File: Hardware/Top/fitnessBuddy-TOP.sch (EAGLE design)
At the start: 52 parts, among them SW3 SWITCH.MOM, SW4 SWITCH.MOM, U1 NRF52832_MODULE_MDBT42, U2 FT231XS

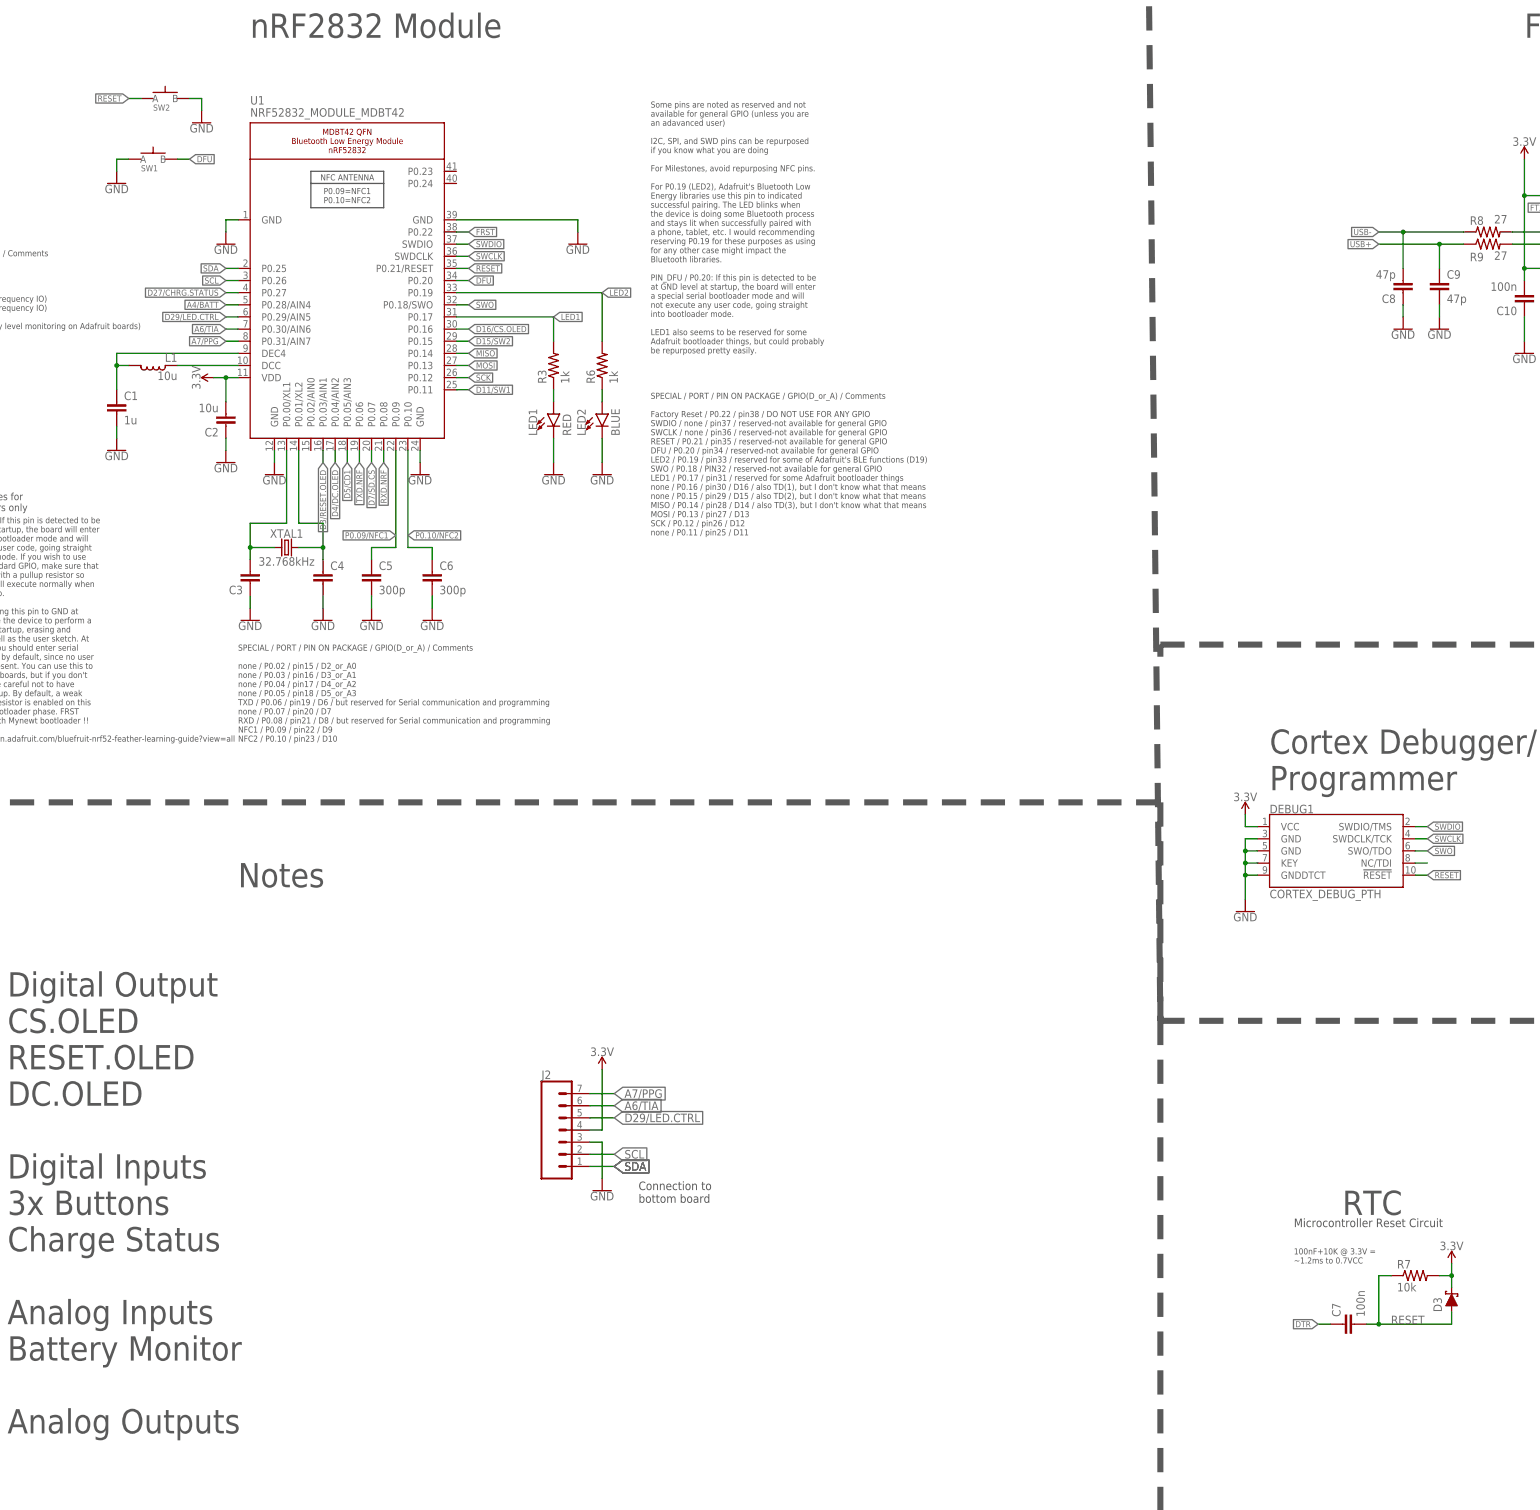
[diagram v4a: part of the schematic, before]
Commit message: routed top board
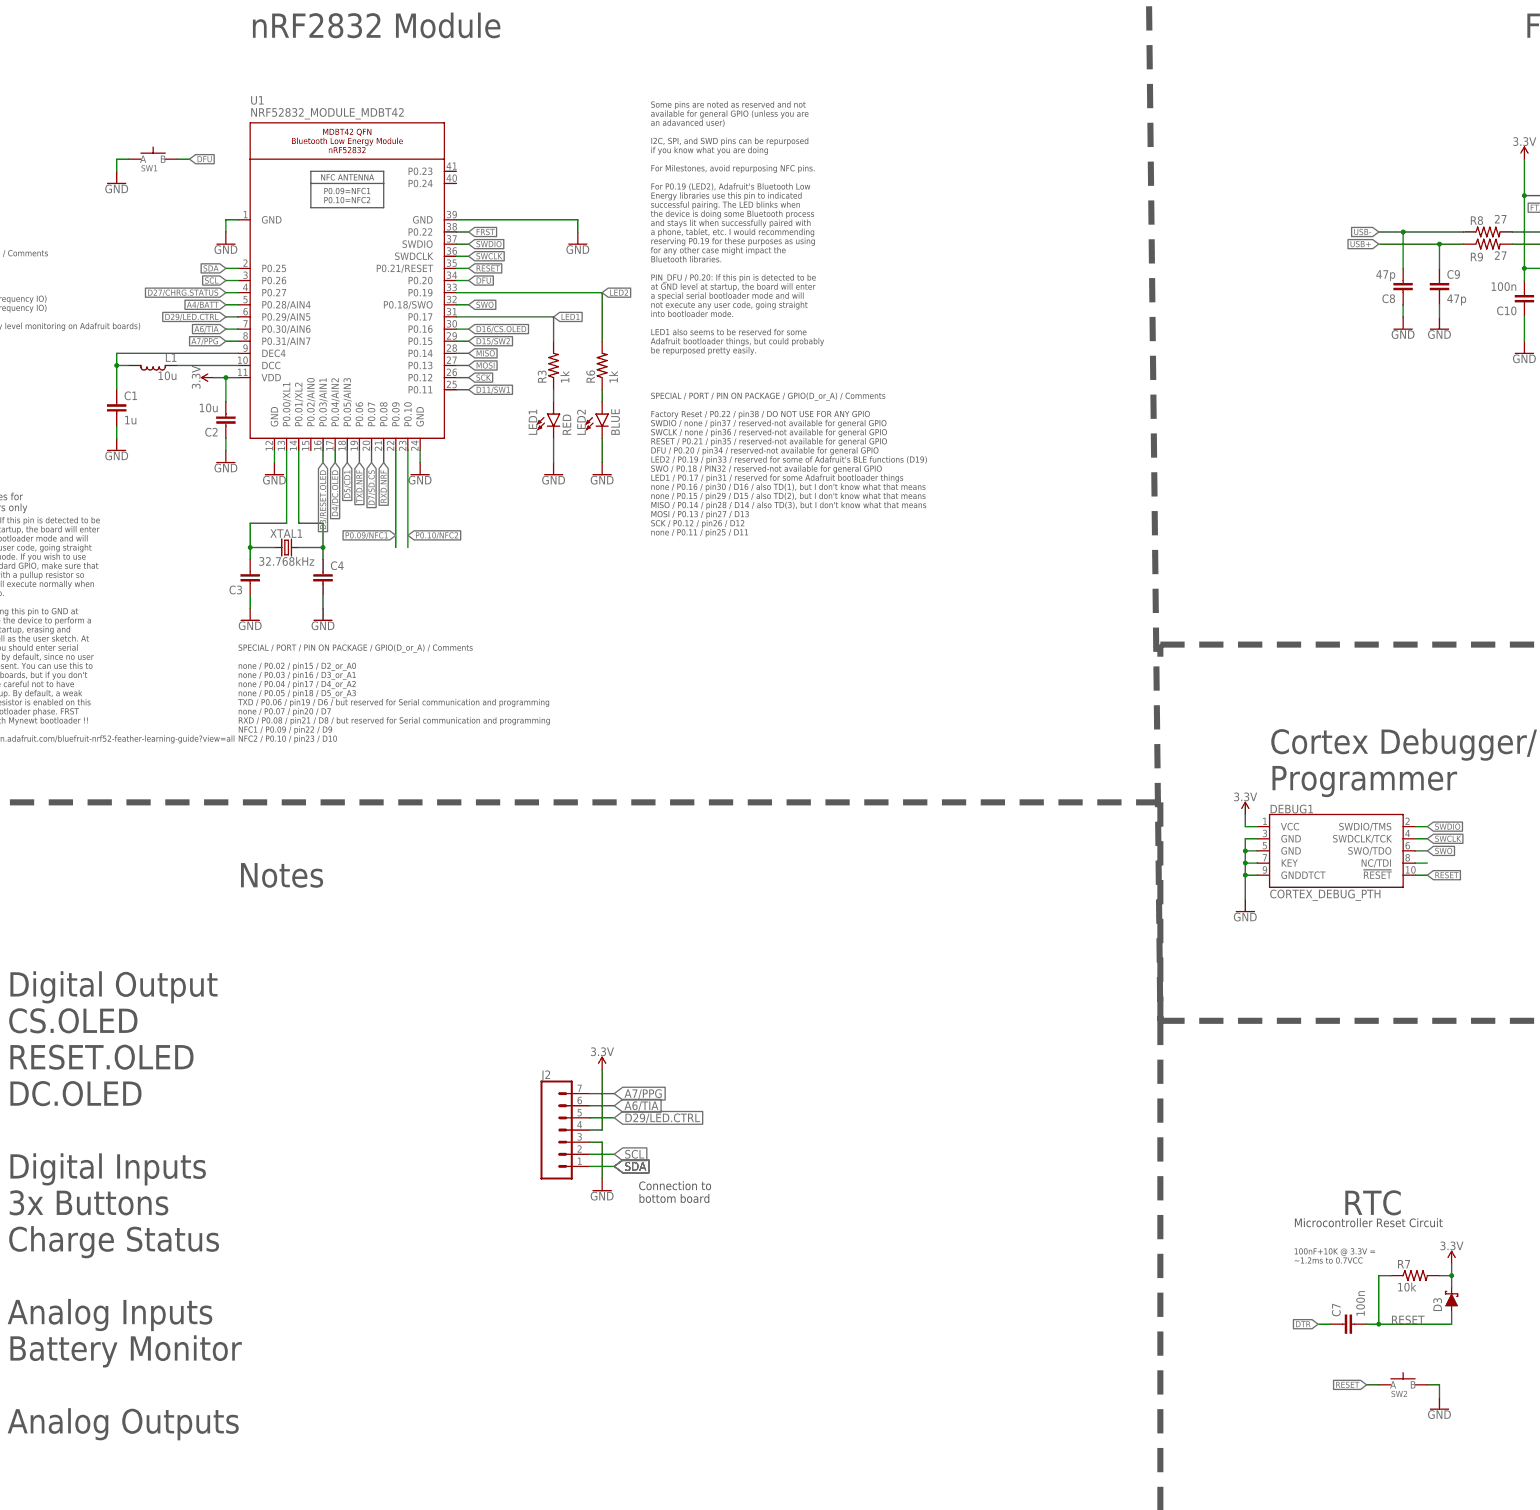
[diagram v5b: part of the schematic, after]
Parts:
- removed C5, C6: 300p, LinnesLab-Passives:CAPACITOR0603
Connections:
- net GND: no longer C5.2, C6.2
- net P0.09/NFC1: no longer C5.1
- net P0.10/NFC2: no longer C6.1
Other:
- moved on the sheet: SW2
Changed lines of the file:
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@@
 <part name="GND15" library="LinnesLab-Symbols" deviceset="GND" device=""/>
 <part name="GND16" library="LinnesLab-Symbols" deviceset="GND" device=""/>
-<part name="GND17" library="LinnesLab-Symbols" deviceset="GND" device=""/>
-<part name="GND18" library="LinnesLab-Symbols" deviceset="GND" device=""/>
 <part name="GND19" library="LinnesLab-Symbols" deviceset="GND" device=""/>
 <part name="GND20" library="LinnesLab-Symbols" deviceset="GND" device=""/>
@@
 <part name="C3" library="LinnesLab-Passives" deviceset="CAPACITOR" device="0603" package3d_urn="urn:adsk.eagle:package:15661989/2"/>
 <part name="C4" library="LinnesLab-Passives" deviceset="CAPACITOR" device="0603" package3d_urn="urn:adsk.eagle:package:15661989/2"/>
-<part name="C6" library="LinnesLab-Passives" deviceset="CAPACITOR" device="0603" package3d_urn="urn:adsk.eagle:package:15661989/2" value="300p"/>
-<part name="C5" library="LinnesLab-Passives" deviceset="CAPACITOR" device="0603" package3d_urn="urn:adsk.eagle:package:15661989/2" value="300p"/>
 <part name="C2" library="LinnesLab-Passives" deviceset="CAPACITOR" device="0805" package3d_urn="urn:adsk.eagle:package:15662010/2" value="10u"/>
 <part name="L1" library="LinnesLab-Passives" deviceset="INDUCTOR" device="0603" override_package3d_urn="urn:adsk.eagle:package:18592195/2" override_package_urn="urn:adsk.eagle:footprint:18592196/1" value="10u"/>
@@
 <attribute name="VALUE" x="53.34" y="335.026" size="1.778" layer="96" align="top-center"/>
 </instance>
-<instance part="GND17" gate="G$1" x="55.88" y="304.8" smashed="yes">
-<attribute name="VALUE" x="55.88" y="304.546" size="1.778" layer="96" align="top-center"/>
-</instance>
-<instance part="GND18" gate="G$1" x="43.18" y="304.8" smashed="yes">
-<attribute name="VALUE" x="43.18" y="304.546" size="1.778" layer="96" align="top-center"/>
-</instance>
 <instance part="GND19" gate="G$1" x="33.02" y="304.8" smashed="yes">
 <attribute name="VALUE" x="33.02" y="304.546" size="1.778" layer="96" align="top-center"/>
@@
 <attribute name="VALUE" x="34.544" y="310.261" size="1.778" layer="96"/>
 </instance>
-<instance part="C6" gate="G$1" x="55.88" y="312.42" smashed="yes">
-<attribute name="NAME" x="57.404" y="315.341" size="1.778" layer="95"/>
-<attribute name="VALUE" x="57.404" y="310.261" size="1.778" layer="96"/>
-</instance>
-<instance part="C5" gate="G$1" x="43.18" y="312.42" smashed="yes">
-<attribute name="NAME" x="44.704" y="315.341" size="1.778" layer="95"/>
-<attribute name="VALUE" x="44.704" y="310.261" size="1.778" layer="96"/>
-</instance>
 <instance part="C2" gate="G$1" x="12.7" y="347.98" smashed="yes" rot="R180">
 <attribute name="NAME" x="11.176" y="345.059" size="1.778" layer="95" rot="R180"/>
@@
 <attribute name="VALUE" x="269.24" y="172.974" size="1.778" layer="96" align="bottom-center"/>
 </instance>
-<instance part="GND28" gate="G$1" x="7.62" y="408.94" smashed="yes">
-<attribute name="VALUE" x="7.62" y="408.686" size="1.778" layer="96" align="top-center"/>
+<instance part="GND28" gate="G$1" x="266.7" y="139.7" smashed="yes">
+<attribute name="VALUE" x="266.7" y="139.446" size="1.778" layer="96" align="top-center"/>
 </instance>
 <instance part="SUPPLY5" gate="G$1" x="226.06" y="264.16" smashed="yes">
@@
 <attribute name="VALUE" x="22.86" y="335.026" size="1.778" layer="96" align="top-center"/>
 </instance>
-<instance part="SW2" gate="G$1" x="0" y="414.02" smashed="yes">
-<attribute name="NAME" x="-2.54" y="411.48" size="1.27" layer="95"/>
-<attribute name="VALUE" x="-2.54" y="408.94" size="1.27" layer="96"/>
+<instance part="SW2" gate="G$1" x="259.08" y="144.78" smashed="yes">
+<attribute name="NAME" x="256.54" y="142.24" size="1.27" layer="95"/>
+<attribute name="VALUE" x="256.54" y="139.7" size="1.27" layer="96"/>
 </instance>
 <instance part="U1" gate="G$1" x="38.1" y="375.92" smashed="yes">
@@
 </segment>
 <segment>
-<pinref part="C5" gate="G$1" pin="2"/>
-<pinref part="GND18" gate="G$1" pin="GND"/>
-<wire x1="43.18" y1="307.34" x2="43.18" y2="309.88" width="0.1524" layer="91"/>
-</segment>
-<segment>
-<pinref part="C6" gate="G$1" pin="2"/>
-<pinref part="GND17" gate="G$1" pin="GND"/>
-<wire x1="55.88" y1="307.34" x2="55.88" y2="309.88" width="0.1524" layer="91"/>
-</segment>
-<segment>
 <wire x1="15.24" y1="388.62" x2="12.7" y2="388.62" width="0.1524" layer="91"/>
 <wire x1="12.7" y1="388.62" x2="12.7" y2="386.08" width="0.1524" layer="91"/>
@@
 </segment>
 <segment>
-<wire x1="5.08" y1="414.02" x2="7.62" y2="414.02" width="0.1524" layer="91"/>
-<wire x1="7.62" y1="414.02" x2="7.62" y2="411.48" width="0.1524" layer="91"/>
+<wire x1="264.16" y1="144.78" x2="266.7" y2="144.78" width="0.1524" layer="91"/>
+<wire x1="266.7" y1="144.78" x2="266.7" y2="142.24" width="0.1524" layer="91"/>
 <pinref part="GND28" gate="G$1" pin="GND"/>
 <pinref part="SW2" gate="G$1" pin="B"/>
@@
 </segment>
 <segment>
-<wire x1="-7.62" y1="414.02" x2="-5.08" y2="414.02" width="0.1524" layer="91"/>
-<label x="-7.62" y="414.02" size="1.27" layer="95" rot="R180" xref="yes"/>
+<wire x1="251.46" y1="144.78" x2="254" y2="144.78" width="0.1524" layer="91"/>
+<label x="251.46" y="144.78" size="1.27" layer="95" rot="R180" xref="yes"/>
 <pinref part="SW2" gate="G$1" pin="A"/>
 </segment>
@@
 <segment>
 <wire x1="48.26" y1="340.36" x2="48.26" y2="320.04" width="0.1524" layer="91"/>
-<wire x1="43.18" y1="320.04" x2="48.26" y2="320.04" width="0.1524" layer="91"/>
-<wire x1="43.18" y1="320.04" x2="43.18" y2="317.5" width="0.1524" layer="91"/>
-<pinref part="C5" gate="G$1" pin="1"/>
 <pinref part="U1" gate="G$1" pin="P0.09"/>
 <label x="48.26" y="322.58" size="1.27" layer="95" rot="R180" xref="yes"/>
@@
 <segment>
 <wire x1="50.8" y1="340.36" x2="50.8" y2="320.04" width="0.1524" layer="91"/>
-<wire x1="50.8" y1="320.04" x2="55.88" y2="320.04" width="0.1524" layer="91"/>
-<wire x1="55.88" y1="320.04" x2="55.88" y2="317.5" width="0.1524" layer="91"/>
-<pinref part="C6" gate="G$1" pin="1"/>
 <pinref part="U1" gate="G$1" pin="P0.10"/>
 <label x="50.8" y="322.58" size="1.27" layer="95" xref="yes"/>

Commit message: finished halfway through take 007. organized board/ connected airwires
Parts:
- C13: device LinnesLab-Passives:CAPACITOR0402 -> LinnesLab-Passives:CAPACITOR0603
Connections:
- removed net !DTR: U2.!DTR
- removed net A4/BATT: R4.1, R5.2, U1.P0.28/AIN4
- removed net A6/TIA: J2.6, U1.P0.30/AIN6
- removed net A7/PPG: J2.7, U1.P0.31/AIN7
- removed net D29/LED.CTRL: J2.5, U1.P0.29/AIN5
- new net A4/PPG: J2.7, U1.P0.28/AIN4
- new net A5/TIA: J2.6, U1.P0.29/AIN5
- new net A7/BATT: R4.1, R5.2, U1.P0.31/AIN7
- new net D30/LED.CTRL: J2.5, U1.P0.30/AIN6
- net DTR: now also U2.!DTR
- net GND: no longer SW3.4, SW4.4

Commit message: organized top board
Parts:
- added C17, C18: 4.7u, LinnesLab-Passives:CAPACITOR0603
- added C5, C6: 1u, LinnesLab-Passives:CAPACITOR0603
- added CHRG2: MCP73831, LinnesLab-Power:MCP73831
- added LDO2: MIC5504, LinnesLab-Power:MIC5504
- added R16: (no value), LinnesLab-Passives:RESISTOR0603
- added R17: 100k, LinnesLab-Passives:RESISTOR0603
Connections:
- new net N$16: CHRG2.PROG, R16.2
- new net N$17: C18.2, CHRG2.VIN, R17.2
- net 3.3V: now also C6.1, LDO2.OUT
- net D27/CHRG.STATUS: now also CHRG2.STAT, R17.1
- net GND: now also C17.2, C18.1, C5.1, C6.2, CHRG2.VSS, LDO2.GND, R16.1
- net VIN: now also C5.2, LDO2.EN, LDO2.IN
- net VLIPO: now also C17.1, CHRG2.VBAT
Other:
- note added: "Digital Output"

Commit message: reorganized bottom boards, added RTC to bottom board, and added notes to top schematic
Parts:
- C10: value 100n -> 47p
- C11: value 10uF -> 47p
- C12: value 2.2uF -> 100n; device LinnesLab-Passives:CAPACITOR0402 -> LinnesLab-Passives:CAPACITOR0603
- C13: value 2.2uF -> 10uF
- C15: device LinnesLab-Passives:CAPACITOR0402 -> LinnesLab-Passives:CAPACITOR0603
- C17, C18: value 4.7u -> 2.2uF; device LinnesLab-Passives:CAPACITOR0603 -> LinnesLab-Passives:CAPACITOR0402
- C5: value 1u -> 4.7u
- C7: value 100n -> 1u
- C8: value 47p -> 4.7u
- C9: value 47p -> 100n
- R10: value 10k -> 27
- R11: value 1k -> 27
- R12: value 390k -> 10k
- R14: value 0 -> 390k
- R15: value 0 -> 1k
- R16: value (none) -> 0
- R17: value 100k -> 0
- R7: value 10k -> 100k
- R8: value 27 -> 5k
- R9: value 27 -> 10k
- renumbered CHRG2 to CHRG1, LDO2 to LDO1, SW2 to RESET
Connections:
- net 3.3V: now also C12.2, C17.2, C18.2, C7.1, R9.2; no longer C10.2, C15.2, C16.2, C6.1, R7.2
- net D27/CHRG.STATUS: now also R7.1; no longer R17.1
- net DTR: now also C9.1; no longer C7.1
- net GND: now also C11.2, C12.1, C17.1, C6.1, C7.2, C8.2, R12.1, R14.2, R8.1; no longer C11.1, C16.1, C17.2, C6.2, C8.1, C9.2, R10.1, R12.2, R16.1
- net N$1: now also R12.2; no longer R10.2
- net N$13: now also C13.2; no longer C11.2
- net N$15: now also C15.2; no longer C13.2
- net N$16: now also R8.2; no longer R16.2
- net N$17: now also C5.2, R7.2; no longer C18.2, R17.2
- net N$2: now also R14.1; no longer R12.1
- net N$23: now also R10.2; no longer R8.2
- net N$24: now also R11.2; no longer R9.2
- net N$25: now also R13.2; no longer R11.2
- net N$26: now also R15.2; no longer R13.2
- net N$3: now also C16.2; no longer C14.2
- net N$5: now also C16.1; no longer C14.1
- net N$7: now also C14.2; no longer C12.2
- net N$8: now also C14.1; no longer C12.1
- net RESET: now also C9.2, R9.1; no longer C7.2, R7.1
- net RXD.FT: now also R17.1; no longer R15.1
- net RXD.NRF: now also R16.2; no longer R14.2
- net RXLED: now also R13.1; no longer R11.1
- net TXD.FT: now also R16.1; no longer R14.1
- net TXD.NRF: now also R17.2; no longer R15.2
- net TXLED: now also R15.1; no longer R13.1
- net USB+: now also C11.1, R11.1; no longer C9.1, R9.1
- net USB-: now also C10.2, R10.1; no longer C8.2, R8.1
- net VIN: now also C6.2; no longer C5.2
- net VLIPO: now also C8.1; no longer C17.1
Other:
- note added: "Diodes switch from LiPo power to USB when USB is connected The USB power then charges the battery"
- note added: "Fitness Buddy Basic Top Revision A Date: Monday, October 19th Author: Vishank Battar"
- note added: "Headers connecting top and bottom boards"
- note added: "voltage divider used to monitor battery voltage"
- note removed: "RTC"
- moved on the sheet: C10, C11, C12, C13, C14, C15, C16, C17, C18, C5, C6, C7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
